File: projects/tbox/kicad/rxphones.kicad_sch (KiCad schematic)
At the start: 0 parts

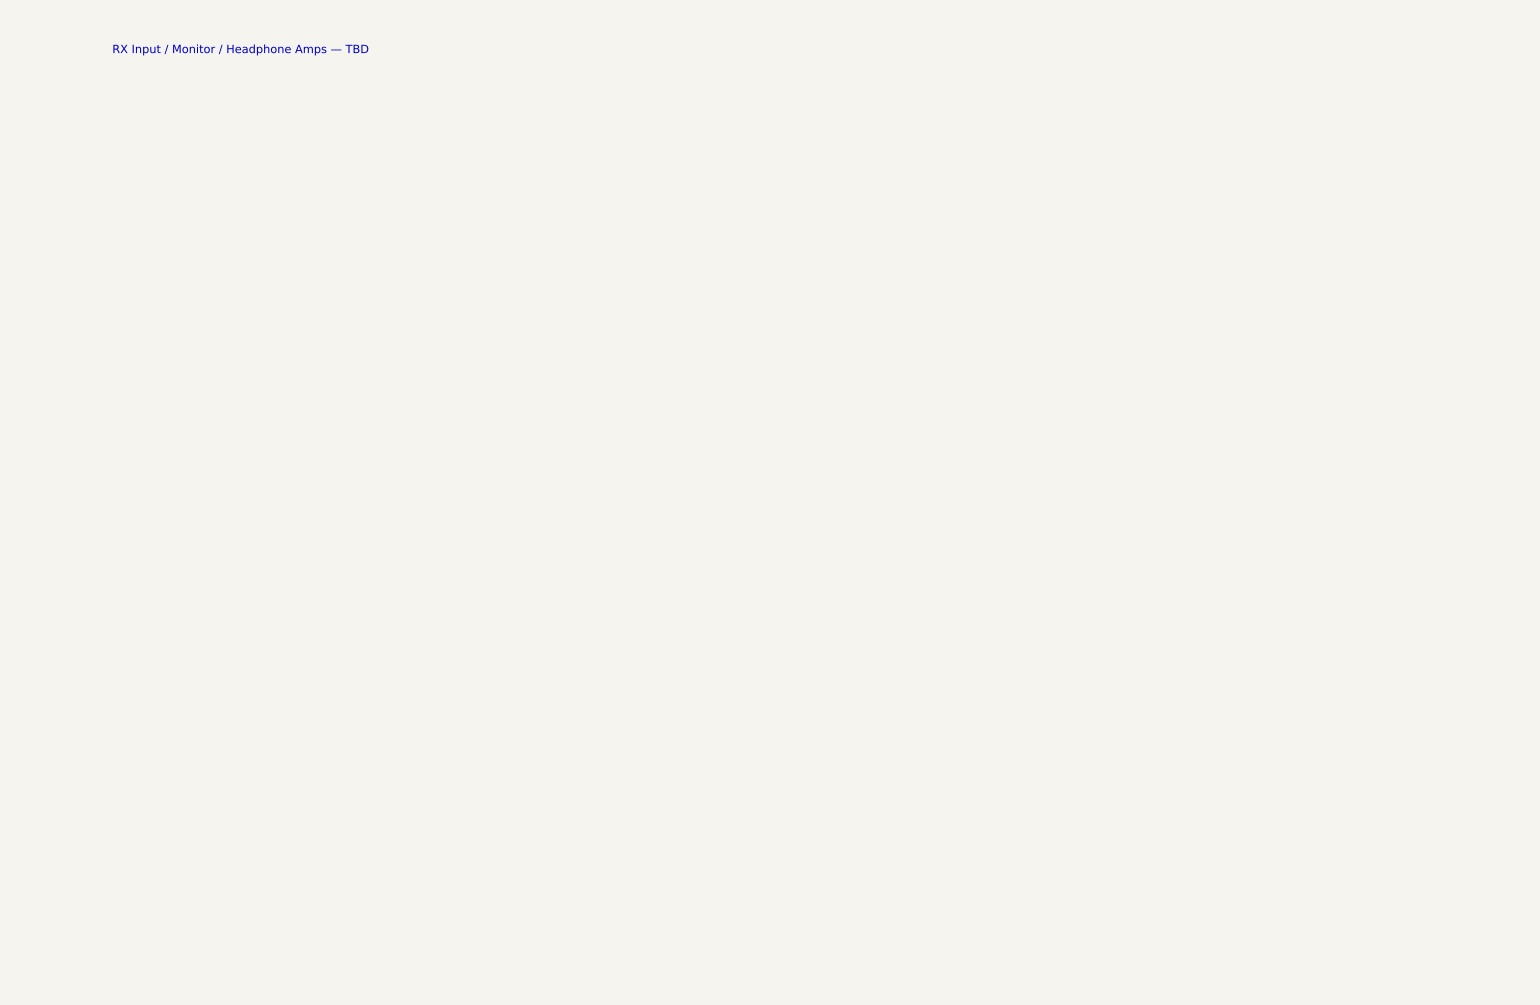
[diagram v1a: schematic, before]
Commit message: Complete the TX Bus, RX+Phones and Keying sheets; adversarial review fixes
Schematic
- New sheets: TX Bus (summing, intercom mute, mic/line out), RX + Phones,
  Keying + Rear (PTT, override, DE-9 with protection, indicators, rear
  switches, power-on mute hold).
- Mute is a shared sub-sheet (mute.kicad_sch) instanced in each preamp
  and the intercom.  Started as a JFET series+shunt pair; replaced by a
  TS12A12511 SPDT to VREF because a worst-case J113 is not pinched off
  inside the 9 V window at 0 dBV peaks.
- Preamp: TS12A12511 gain select (was DG419), HI +40 / LO +20 dB, RF
  entry filters, bias decoupling, feedback returns to GND.
- Supply: TPS7A4701 (ANY-OUT 9.0 V) replaces the LM2940, SMBJ18A input
  TVS, entry ceramics, VREF stiffened.
- VREF is DC bias only; every gain-setting leg returns to GND.
- CHASSIS net for all sleeves/returns with a single net tie; rear GND
  post; isolated line-out secondaries return to the jack sleeve.
- Keying logic transistors are 2N7002 so logic highs stay above ~7 V
  (the analog-switch VIH is 5 V guaranteed at 12 V); hold re-armed by a
  clamp diode.
- Test points on every sheet; title blocks rev 0.2.

Tooling and docs
- tools/check_sch.py: geometric lint for pins on wire interiors,
  touching pins, T-junctions without a dot, duplicate references.
- power_tree.json / Load_mA updated for the new regulator and loads.
- DESIGN.md, LEVELS.md, TODO.md brought in line (DRY trim, corrected
  numbers, open items); rear panel LINE L / LINE R.
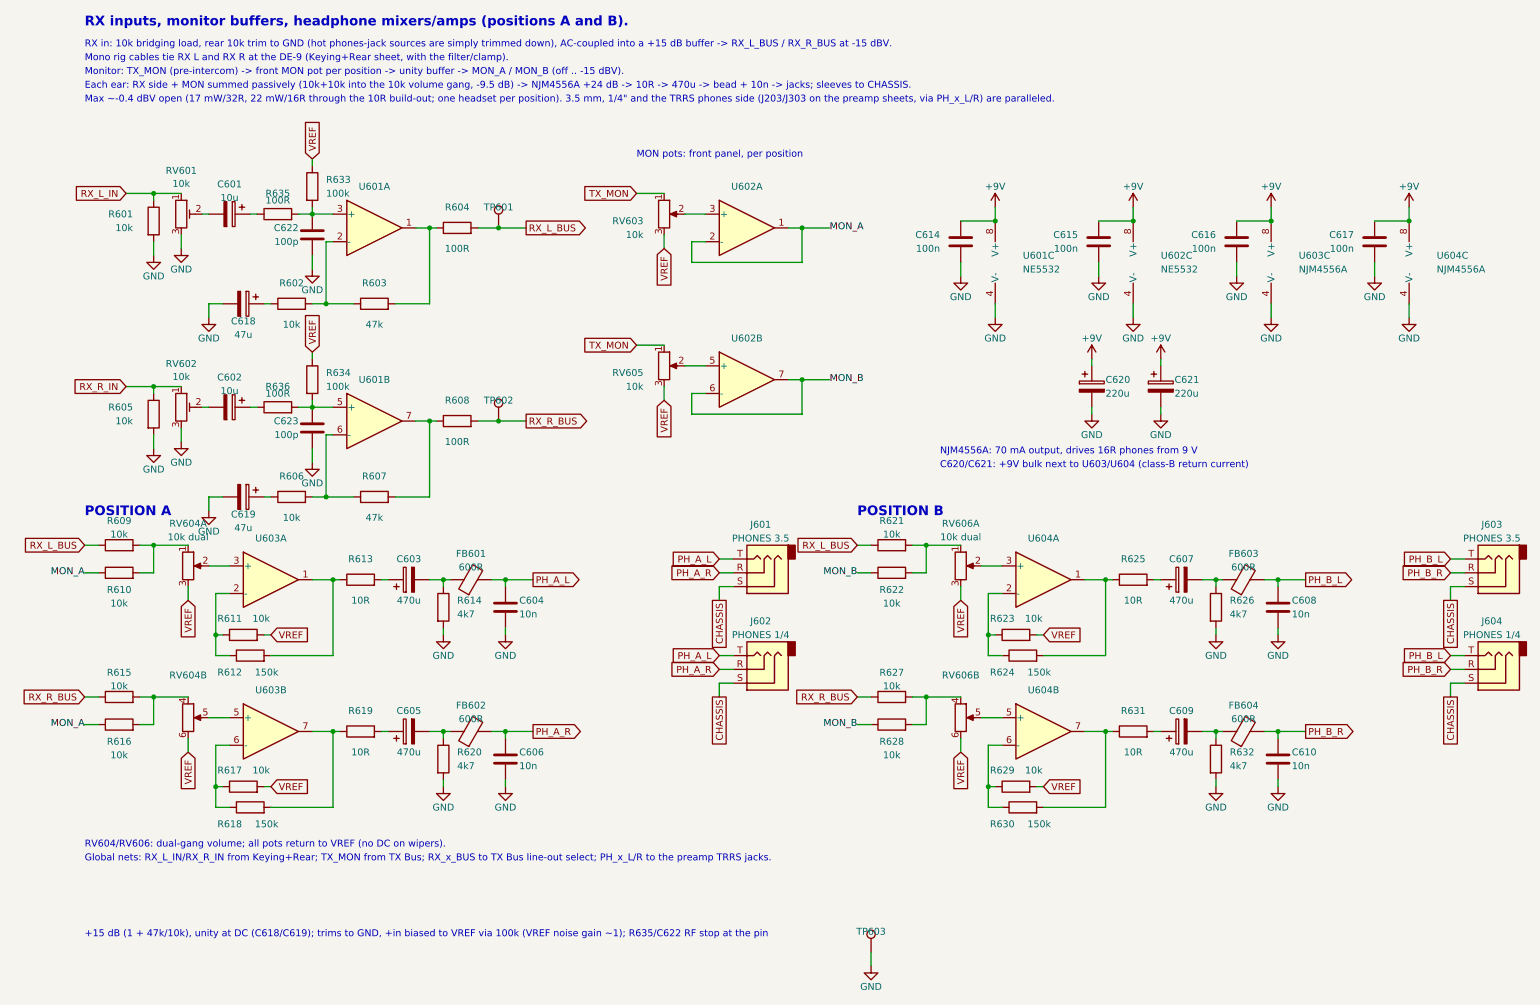
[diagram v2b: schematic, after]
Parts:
- added C601, C602: 10u, symbol Device:C_Polarized
- added C603, C605, C607, C609: 470u, symbol Device:C_Polarized
- added C604, C606, C608, C610: 10n, symbol Device:C
- added C614, C615, C616, C617: 100n, symbol Device:C
- added C618, C619: 47u, symbol Device:C_Polarized
- added C620, C621: 220u, symbol Device:C_Polarized
- added C622, C623: 100p, symbol Device:C
- added FB601, FB602, FB603, FB604: 600R, symbol Device:FerriteBead
- added J601, J603: PHONES 3.5, symbol Connector_Audio:AudioJack3
- added J602, J604: PHONES 1/4, symbol Connector_Audio:AudioJack3
- added R601, R602, R605, R606, R609, R610, R611, R615, R616, R617, R621, R622, R623, R627, R628, R629: 10k, symbol Device:R
- added R603, R607: 47k, symbol Device:R
- added R604, R608, R635, R636: 100R, symbol Device:R
- added R612, R618, R624, R630: 150k, symbol Device:R
- added R613, R619, R625, R631: 10R, symbol Device:R
- added R614, R620, R626, R632: 4k7, symbol Device:R
- added R633, R634: 100k, symbol Device:R
- added RV601, RV602: 10k, symbol Device:R_Potentiometer_Trim
- added RV603, RV605: 10k, symbol Device:R_Potentiometer
- added RV604, RV606: 10k dual, symbol Device:R_Potentiometer_Dual_Separate
- added TP601: RX_L_BUS, symbol Connector:TestPoint
- added TP602: RX_R_BUS, symbol Connector:TestPoint
- added TP603: GND, symbol Connector:TestPoint
- added U601, U602: NE5532, symbol tbox:NE5532
- added U603, U604: NJM4556A, symbol tbox:NJM4556A
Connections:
- new net: C619.1, R606.1
- new net: R606.2, R607.1, U601.6 (-)
- new net: C618.1, R602.1
- new net: R602.2, R603.1, U601.2 (-)
- new net: RV603.2, U602.3 (+)
- new net: C623.1, R634.2, R636.2, U601.5 (+)
- new net: R607.2, R608.1, U601.7
- new net: R629.1, R630.1, U604.6 (-)
- new net: R621.2, R622.2, RV606.1
- new net: C607.2, FB603.1, R626.1
- new net: C603.2, FB601.1, R614.1
- new net: RV606.2, U604.3 (+)
- new net: R617.1, R618.1, U603.6 (-)
- new net: R624.2, R625.1, U604.1
- new net: C607.1, R625.2
- new net: R623.1, R624.1, U604.2 (-)
- new net: R615.2, R616.2, RV604.4
- new net: R618.2, R619.1, U603.7
- new net: R627.2, R628.2, RV606.4
- new net: RV606.5, U604.5 (+)
- new net: C605.2, FB602.1, R620.1
- new net: RV604.5, U603.5 (+)
- new net: R609.2, R610.2, RV604.1
- new net: C602.2, RV602.2
- new net: C609.1, R631.2
- new net: C609.2, FB604.1, R632.1
- new net: R611.1, R612.1, U603.2 (-)
- new net: C605.1, R619.2
- new net: R612.2, R613.1, U603.1
- new net: C603.1, R613.2
- new net: R603.2, R604.1, U601.1
- new net: C622.1, R633.2, R635.2, U601.3 (+)
- new net: C602.1, R636.1
- new net: RV604.2, U603.3 (+)
- new net: R630.2, R631.1, U604.7
- new net: RV605.2, U602.5 (+)
- new net: C601.2, RV601.2
- new net: C601.1, R635.1
- new net +9V: C614.1, C615.1, C616.1, C617.1, C620.1, C621.1, U601.8 (V+), U602.8 (V+), U603.8 (V+), U604.8 (V+)
- new net CHASSIS: J601.S, J602.S, J603.S, J604.S
- new net GND: C604.2, C606.2, C608.2, C610.2, C614.2, C615.2, C616.2, C617.2, C618.2, C619.2, C620.2, C621.2, C622.2, C623.2, R601.2, R605.2, R614.2, R620.2, R626.2, R632.2, RV601.3, RV602.3, TP603.1, U601.4 (V-), U602.4 (V-), U603.4 (V-), U604.4 (V-)
- new net MON_A: R610.1, R616.1, U602.1, U602.2 (-)
- new net MON_B: R622.1, R628.1, U602.6 (-), U602.7
- new net PH_A_L: C604.1, FB601.2, J601.T, J602.T
- new net PH_A_R: C606.1, FB602.2, J601.R, J602.R
- new net PH_B_L: C608.1, FB603.2, J603.T, J604.T
- new net PH_B_R: C610.1, FB604.2, J603.R, J604.R
- new net RX_L_BUS: R604.2, R609.1, R621.1, TP601.1
- new net RX_L_IN: R601.1, RV601.1
- new net RX_R_BUS: R608.2, R615.1, R627.1, TP602.1
- new net RX_R_IN: R605.1, RV602.1
- new net TX_MON: RV603.1, RV605.1
- new net VREF: R611.2, R617.2, R623.2, R629.2, R633.1, R634.1, RV603.3, RV604.3, RV604.6, RV605.3, RV606.3, RV606.6
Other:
- note added: "+15 dB (1 + 47k/10k), unity at DC (C618/C619); trims to GND, +in biased to VREF via 100k (VREF noise gain ~1); R635/C622 RF stop at the pin"
- note added: "C620/C621: +9V bulk next to U603/U604 (class-B return current)"
- note added: "Each ear: RX side + MON summed passively (10k+10k into the 10k volume gang, -9.5 dB) -> NJM4556A +24 dB -> 10R -> 470u -> bead + 10n -> jacks; sleeves to CHASSIS."
- note added: "Global nets: RX_L_IN/RX_R_IN from Keying+Rear; TX_MON from TX Bus; RX_x_BUS to TX Bus line-out select; PH_x_L/R to the preamp TRRS jacks."
- note added: "MON pots: front panel, per position"
- note added: "Max ~-0.4 dBV open (17 mW/32R, 22 mW/16R through the 10R build-out; one headset per position). 3.5 mm, 1/4" and the TRRS phones side (J203/J303 on the preamp sheets, via PH_x_L/R) are paralleled."
- note added: "Monitor: TX_MON (pre-intercom) -> front MON pot per position -> unity buffer -> MON_A / MON_B (off .. -15 dBV)."
- note added: "Mono rig cables tie RX L and RX R at the DE-9 (Keying+Rear sheet, with the filter/clamp)."
- note added: "NJM4556A: 70 mA output, drives 16R phones from 9 V"
- note added: "POSITION A"
- note added: "POSITION B"
- note added: "RV604/RV606: dual-gang volume; all pots return to VREF (no DC on wipers)."
- note added: "RX in: 10k bridging load, rear 10k trim to GND (hot phones-jack sources are simply trimmed down), AC-coupled into a +15 dB buffer -> RX_L_BUS / RX_R_BUS at -15 dBV."
- note added: "RX inputs, monitor buffers, headphone mixers/amps (positions A and B)."
- note removed: "RX Input / Monitor / Headphone Amps — TBD"
- title: TBox — RX Input / Monitor / Headphone Amps -> TBox — RX Inputs / Monitor / Headphones

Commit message: Replace NE5532 with OPA1678; annotate logic pull-up loads
The NE5532 is only specified from 10 V total; at 9 V its input
common-mode range works out to 3-6 V (0.1 V of margin at 0 dBV peaks)
and TI no longer specifies its output swing at all.  The OPA1678 is
pin-compatible, specified 4.5-36 V, guarantees the output within 0.8 V
of each rail and a 0.5-7 V input range, has slightly lower noise
(4.5 nV/rtHz) and draws 2 mA/ch instead of up to 8.

- tbox.kicad_sym: OPA1678 symbol replaces NE5532 (all 8 packages).
- Load_mA 4/5 per package, including the previously unannotated
  preamps; PTT inverter pull-ups, mute buttons and the intercom NOR
  are now annotated too (they were the missing "discretes").
- power_tree.json: +9V budget 60 typ / 175 max (was 70/205), Pd note;
  extracted loads now reconcile exactly (174 mA max, 17 parts).
- LEVELS: clip point +8 dBV guaranteed, plan still budgets +6.
  DESIGN/TODO updated; the "measure the 5532 clip" bench item is gone.
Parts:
- U601, U602: value NE5532 -> OPA1678; symbol tbox:NE5532 -> tbox:OPA1678
- U601, U602: value NE5532 -> OPA1678; symbol tbox:NE5532 -> tbox:OPA1678; Load_mA 8/16 -> 4/5
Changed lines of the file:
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@@
       (path "/6a29b3f1-3e67-482d-942d-4557fa8bc2d6/f507c32f-2f77-4dfe-93a9-3121ae78e65b" (reference "#PWR0603") (unit 1))))
   )
-  (symbol (lib_id "tbox:NE5532") (at 73.66 57.15 0) (unit 1)
+  (symbol (lib_id "tbox:OPA1678") (at 73.66 57.15 0) (unit 1)
     (exclude_from_sim no) (in_bom yes) (on_board yes) (dnp no)
     (property "Reference" "U601" (at 73.66 49.53 0) (effects (font (size 1.27 1.27))))
-    (property "Value" "NE5532" (at 73.66 64.77 0) (effects (font (size 1.27 1.27)) (hide yes)))
+    (property "Value" "OPA1678" (at 73.66 64.77 0) (effects (font (size 1.27 1.27)) (hide yes)))
     (property "Footprint" "" (at 73.66 57.15 0) (effects (font (size 1.27 1.27)) (hide yes)))
     (property "Datasheet" "" (at 73.66 57.15 0) (effects (font (size 1.27 1.27)) (hide yes)))
@@
       (path "/6a29b3f1-3e67-482d-942d-4557fa8bc2d6/f507c32f-2f77-4dfe-93a9-3121ae78e65b" (reference "#PWR0607") (unit 1))))
   )
-  (symbol (lib_id "tbox:NE5532") (at 73.66 92.71 0) (unit 2)
+  (symbol (lib_id "tbox:OPA1678") (at 73.66 92.71 0) (unit 2)
     (exclude_from_sim no) (in_bom yes) (on_board yes) (dnp no)
     (property "Reference" "U601" (at 73.66 85.09 0) (effects (font (size 1.27 1.27))))
-    (property "Value" "NE5532" (at 73.66 100.33 0) (effects (font (size 1.27 1.27)) (hide yes)))
+    (property "Value" "OPA1678" (at 73.66 100.33 0) (effects (font (size 1.27 1.27)) (hide yes)))
     (property "Footprint" "" (at 73.66 92.71 0) (effects (font (size 1.27 1.27)) (hide yes)))
     (property "Datasheet" "" (at 73.66 92.71 0) (effects (font (size 1.27 1.27)) (hide yes)))
@@
       (path "/6a29b3f1-3e67-482d-942d-4557fa8bc2d6/f507c32f-2f77-4dfe-93a9-3121ae78e65b" (reference "RV603") (unit 1))))
   )
-  (symbol (lib_id "tbox:NE5532") (at 142.24 57.15 0) (unit 1)
+  (symbol (lib_id "tbox:OPA1678") (at 142.24 57.15 0) (unit 1)
     (exclude_from_sim no) (in_bom yes) (on_board yes) (dnp no)
     (property "Reference" "U602" (at 142.24 49.53 0) (effects (font (size 1.27 1.27))))
-    (property "Value" "NE5532" (at 142.24 64.77 0) (effects (font (size 1.27 1.27)) (hide yes)))
+    (property "Value" "OPA1678" (at 142.24 64.77 0) (effects (font (size 1.27 1.27)) (hide yes)))
     (property "Footprint" "" (at 142.24 57.15 0) (effects (font (size 1.27 1.27)) (hide yes)))
     (property "Datasheet" "" (at 142.24 57.15 0) (effects (font (size 1.27 1.27)) (hide yes)))
@@
       (path "/6a29b3f1-3e67-482d-942d-4557fa8bc2d6/f507c32f-2f77-4dfe-93a9-3121ae78e65b" (reference "RV605") (unit 1))))
   )
-  (symbol (lib_id "tbox:NE5532") (at 142.24 85.09 0) (unit 2)
+  (symbol (lib_id "tbox:OPA1678") (at 142.24 85.09 0) (unit 2)
     (exclude_from_sim no) (in_bom yes) (on_board yes) (dnp no)
     (property "Reference" "U602" (at 142.24 77.47 0) (effects (font (size 1.27 1.27))))
-    (property "Value" "NE5532" (at 142.24 92.71 0) (effects (font (size 1.27 1.27)) (hide yes)))
+    (property "Value" "OPA1678" (at 142.24 92.71 0) (effects (font (size 1.27 1.27)) (hide yes)))
     (property "Footprint" "" (at 142.24 85.09 0) (effects (font (size 1.27 1.27)) (hide yes)))
     (property "Datasheet" "" (at 142.24 85.09 0) (effects (font (size 1.27 1.27)) (hide yes)))
@@
       (path "/6a29b3f1-3e67-482d-942d-4557fa8bc2d6/f507c32f-2f77-4dfe-93a9-3121ae78e65b" (reference "U602") (unit 2))))
   )
-  (symbol (lib_id "tbox:NE5532") (at 190.5 63.5 0) (unit 3)
+  (symbol (lib_id "tbox:OPA1678") (at 190.5 63.5 0) (unit 3)
     (exclude_from_sim no) (in_bom yes) (on_board yes) (dnp no)
     (property "Reference" "U601" (at 193.04 62.23 0) (effects (font (size 1.27 1.27)) (justify left)))
-    (property "Value" "NE5532" (at 193.04 64.77 0) (effects (font (size 1.27 1.27)) (justify left)))
+    (property "Value" "OPA1678" (at 193.04 64.77 0) (effects (font (size 1.27 1.27)) (justify left)))
     (property "Footprint" "" (at 190.5 63.5 0) (effects (font (size 1.27 1.27)) (hide yes)))
     (property "Datasheet" "" (at 190.5 63.5 0) (effects (font (size 1.27 1.27)) (hide yes)))
     (property "Description" "" (at 190.5 63.5 0) (effects (font (size 1.27 1.27)) (hide yes)))
-    (property "Load_mA" "8/16" (at 190.5 63.5 0) (effects (font (size 1.27 1.27)) (hide yes)))
+    (property "Load_mA" "4/5" (at 190.5 63.5 0) (effects (font (size 1.27 1.27)) (hide yes)))
     (pin "4")
     (pin "8")
@@
       (path "/6a29b3f1-3e67-482d-942d-4557fa8bc2d6/f507c32f-2f77-4dfe-93a9-3121ae78e65b" (reference "#PWR0611") (unit 1))))
   )
-  (symbol (lib_id "tbox:NE5532") (at 215.9 63.5 0) (unit 3)
+  (symbol (lib_id "tbox:OPA1678") (at 215.9 63.5 0) (unit 3)
     (exclude_from_sim no) (in_bom yes) (on_board yes) (dnp no)
     (property "Reference" "U602" (at 218.44 62.23 0) (effects (font (size 1.27 1.27)) (justify left)))
-    (property "Value" "NE5532" (at 218.44 64.77 0) (effects (font (size 1.27 1.27)) (justify left)))
+    (property "Value" "OPA1678" (at 218.44 64.77 0) (effects (font (size 1.27 1.27)) (justify left)))
     (property "Footprint" "" (at 215.9 63.5 0) (effects (font (size 1.27 1.27)) (hide yes)))
     (property "Datasheet" "" (at 215.9 63.5 0) (effects (font (size 1.27 1.27)) (hide yes)))
     (property "Description" "" (at 215.9 63.5 0) (effects (font (size 1.27 1.27)) (hide yes)))
-    (property "Load_mA" "8/16" (at 215.9 63.5 0) (effects (font (size 1.27 1.27)) (hide yes)))
+    (property "Load_mA" "4/5" (at 215.9 63.5 0) (effects (font (size 1.27 1.27)) (hide yes)))
     (pin "4")
     (pin "8")

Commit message: Power tree: topology and loads from the schematic, capability from json
power_tree.json now holds only what the schematic cannot know: per-rail
max_ma, its basis and derivation, thresholds.  tools/power_model.py
derives the rail tree from converter pins (power_in -> power_out, or a
Rail_out field where the output reaches the rail through a passive or a
plain output pin) and collects Load_mA per part; both check_power.py
and gen_power_tree.py build on it.

- Rails are flattened: every load is an occurrence on its own rail and
  on each rail upstream (1:1 through linear stages; efficiency + v for
  a switching stage).  RAW_13V8 now reads 68/298 mA rather than the
  48 mA of its direct loads.
- typ/max convention written down (CLAUDE.md, power_model.py); LEDs and
  the intercom NOR annotated as 0/x; phones amps re-rated for the 16 ohm
  headsets LEVELS specifies (10/90 per package, was the 32 ohm 10/53).
  +9V is 62 typ / 250 max, 65 % of the 385 mA thermal cap -- which the
  layout has to earn (TODO records the 2-layer ~250 mA figure).
- Electret bias feeds annotated; VREF declared no_loads by design;
  Rail_out on U2 (RC after VOUT) and U3 (op-amp buffer).
- Tree boxes size to their text; supply-sheet notes get the measured
  load line prepended and were moved off the parts.
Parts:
- U603, U604: Load_mA 10/53 -> 10/90
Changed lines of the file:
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@@
     (property "Datasheet" "" (at 241.3 63.5 0) (effects (font (size 1.27 1.27)) (hide yes)))
     (property "Description" "" (at 241.3 63.5 0) (effects (font (size 1.27 1.27)) (hide yes)))
-    (property "Load_mA" "10/53" (at 241.3 63.5 0) (effects (font (size 1.27 1.27)) (hide yes)))
+    (property "Load_mA" "10/90" (at 241.3 63.5 0) (effects (font (size 1.27 1.27)) (hide yes)))
     (pin "4")
     (pin "8")
@@
     (property "Datasheet" "" (at 266.7 63.5 0) (effects (font (size 1.27 1.27)) (hide yes)))
     (property "Description" "" (at 266.7 63.5 0) (effects (font (size 1.27 1.27)) (hide yes)))
-    (property "Load_mA" "10/53" (at 266.7 63.5 0) (effects (font (size 1.27 1.27)) (hide yes)))
+    (property "Load_mA" "10/90" (at 266.7 63.5 0) (effects (font (size 1.27 1.27)) (hide yes)))
     (pin "4")
     (pin "8")
